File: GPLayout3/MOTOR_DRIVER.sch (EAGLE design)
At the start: 90 parts, among them T1 2N2222, T2 2N2222, U7 ATMEGA328P_TQFP, Y1 16MHz

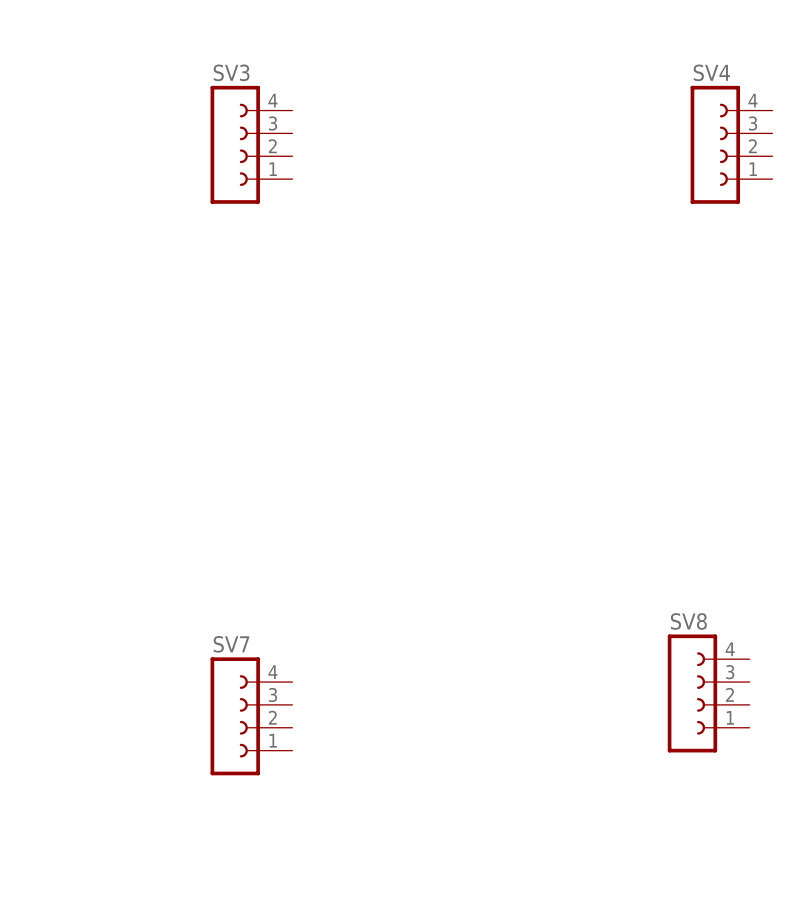
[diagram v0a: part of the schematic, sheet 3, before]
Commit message: Fixed a couple top wires on gate driver chip and gnd
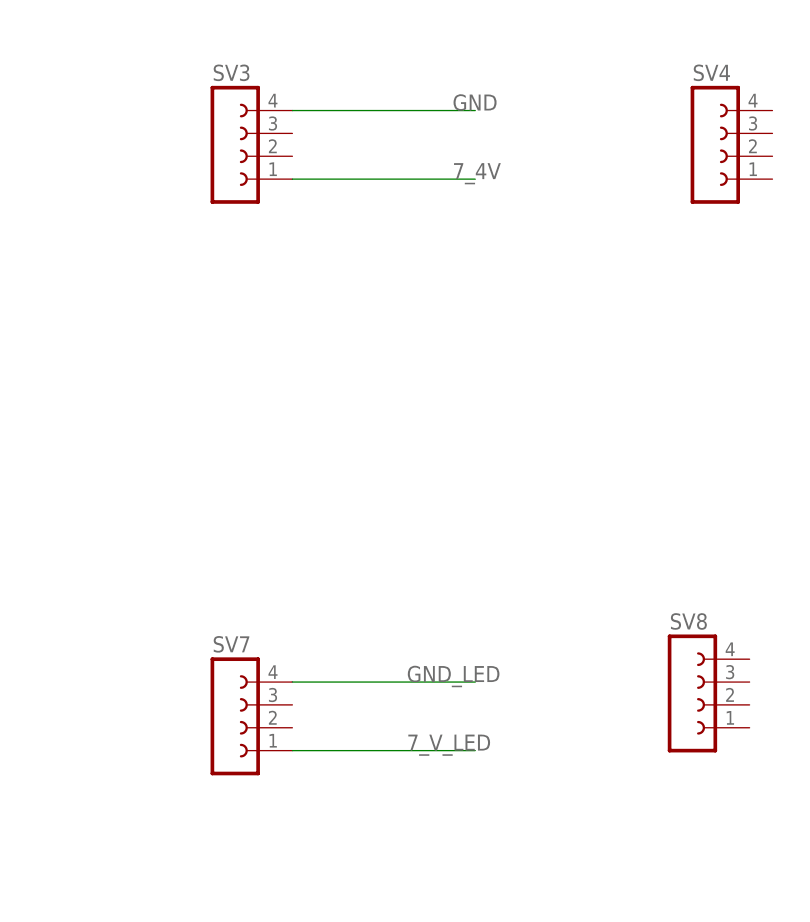
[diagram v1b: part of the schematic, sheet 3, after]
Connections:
- new net 7_V_LED: SV7.1
- new net GND_LED: SV7.4
- net 7_4V: now also SV3.1
- net GND: now also SV3.4
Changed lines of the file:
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@@
 <?xml version="1.0" encoding="utf-8"?>
 <!DOCTYPE eagle SYSTEM "eagle.dtd">
-<eagle version="8.0.1">
+<eagle version="8.0.0">
 <drawing>
 <settings>
@@
 <label x="330.2" y="167.64" size="1.778" layer="95"/>
 </segment>
+<segment>
+<pinref part="SV3" gate="G$1" pin="4"/>
+<wire x1="243.84" y1="226.06" x2="264.16" y2="226.06" width="0.1524" layer="91"/>
+<label x="261.62" y="226.06" size="1.778" layer="95"/>
+</segment>
 </net>
 <net name="5V" class="0">
@@
 <label x="76.2" y="149.86" size="1.778" layer="95"/>
 </segment>
+<segment>
+<pinref part="SV3" gate="G$1" pin="1"/>
+<wire x1="243.84" y1="218.44" x2="264.16" y2="218.44" width="0.1524" layer="91"/>
+<label x="261.62" y="218.44" size="1.778" layer="95"/>
+</segment>
 </net>
 <net name="TX" class="0">
@@
 </segment>
 </net>
+<net name="7_V_LED" class="0">
+<segment>
+<pinref part="SV7" gate="G$1" pin="1"/>
+<wire x1="243.84" y1="154.94" x2="264.16" y2="154.94" width="0.1524" layer="91"/>
+<label x="256.54" y="154.94" size="1.778" layer="95"/>
+</segment>
+</net>
+<net name="GND_LED" class="0">
+<segment>
+<pinref part="SV7" gate="G$1" pin="4"/>
+<wire x1="243.84" y1="162.56" x2="264.16" y2="162.56" width="0.1524" layer="91"/>
+<label x="256.54" y="162.56" size="1.778" layer="95"/>
+</segment>
+</net>

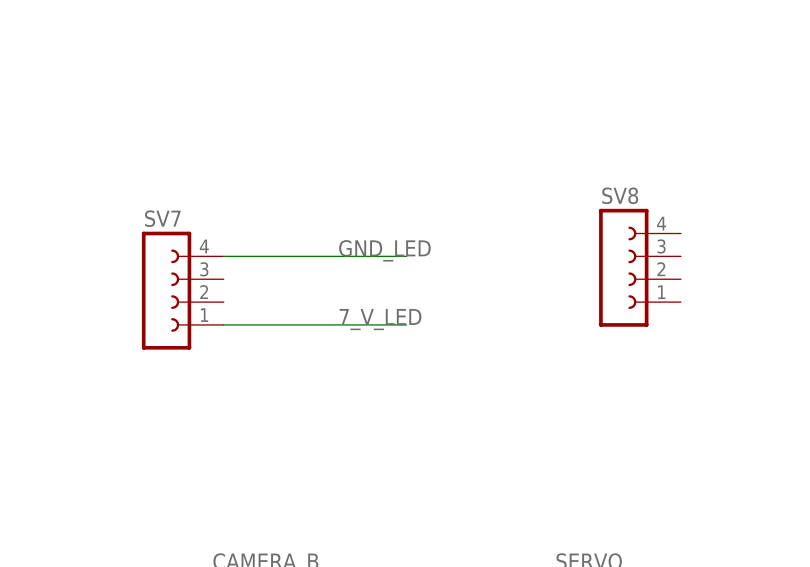
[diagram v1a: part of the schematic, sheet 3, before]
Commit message: Added more wires to top board
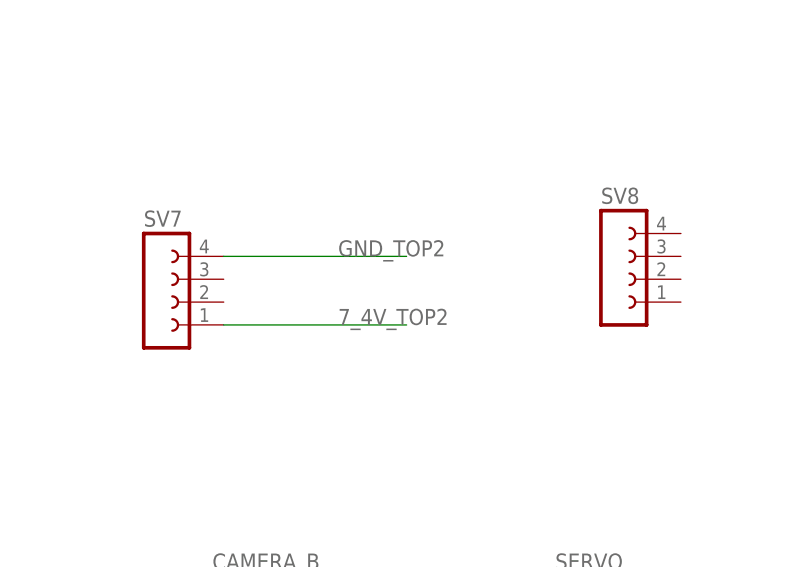
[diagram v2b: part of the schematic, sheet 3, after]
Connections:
- removed net 7_V_LED: SV7.1
- removed net GND_LED: SV7.4
- net 7_4V_TOP2: now also SV7.1
- net GND_TOP2: now also SV7.4
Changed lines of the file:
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@@
 <label x="332.74" y="226.06" size="1.778" layer="95"/>
+</segment>
+<segment>
+<pinref part="SV7" gate="G$1" pin="1"/>
+<wire x1="243.84" y1="154.94" x2="264.16" y2="154.94" width="0.1524" layer="91"/>
+<label x="256.54" y="154.94" size="1.778" layer="95"/>
 </segment>
 </net>
@@
 <wire x1="330.2" y1="223.52" x2="340.36" y2="223.52" width="0.1524" layer="91"/>
 <label x="332.74" y="223.52" size="1.778" layer="95"/>
+</segment>
+<segment>
+<pinref part="SV7" gate="G$1" pin="4"/>
+<wire x1="243.84" y1="162.56" x2="264.16" y2="162.56" width="0.1524" layer="91"/>
+<label x="256.54" y="162.56" size="1.778" layer="95"/>
 </segment>
 </net>
@@
 </segment>
 </net>
-<net name="7_V_LED" class="0">
-<segment>
-<pinref part="SV7" gate="G$1" pin="1"/>
-<wire x1="243.84" y1="154.94" x2="264.16" y2="154.94" width="0.1524" layer="91"/>
-<label x="256.54" y="154.94" size="1.778" layer="95"/>
-</segment>
-</net>
-<net name="GND_LED" class="0">
-<segment>
-<pinref part="SV7" gate="G$1" pin="4"/>
-<wire x1="243.84" y1="162.56" x2="264.16" y2="162.56" width="0.1524" layer="91"/>
-<label x="256.54" y="162.56" size="1.778" layer="95"/>
-</segment>
-</net>

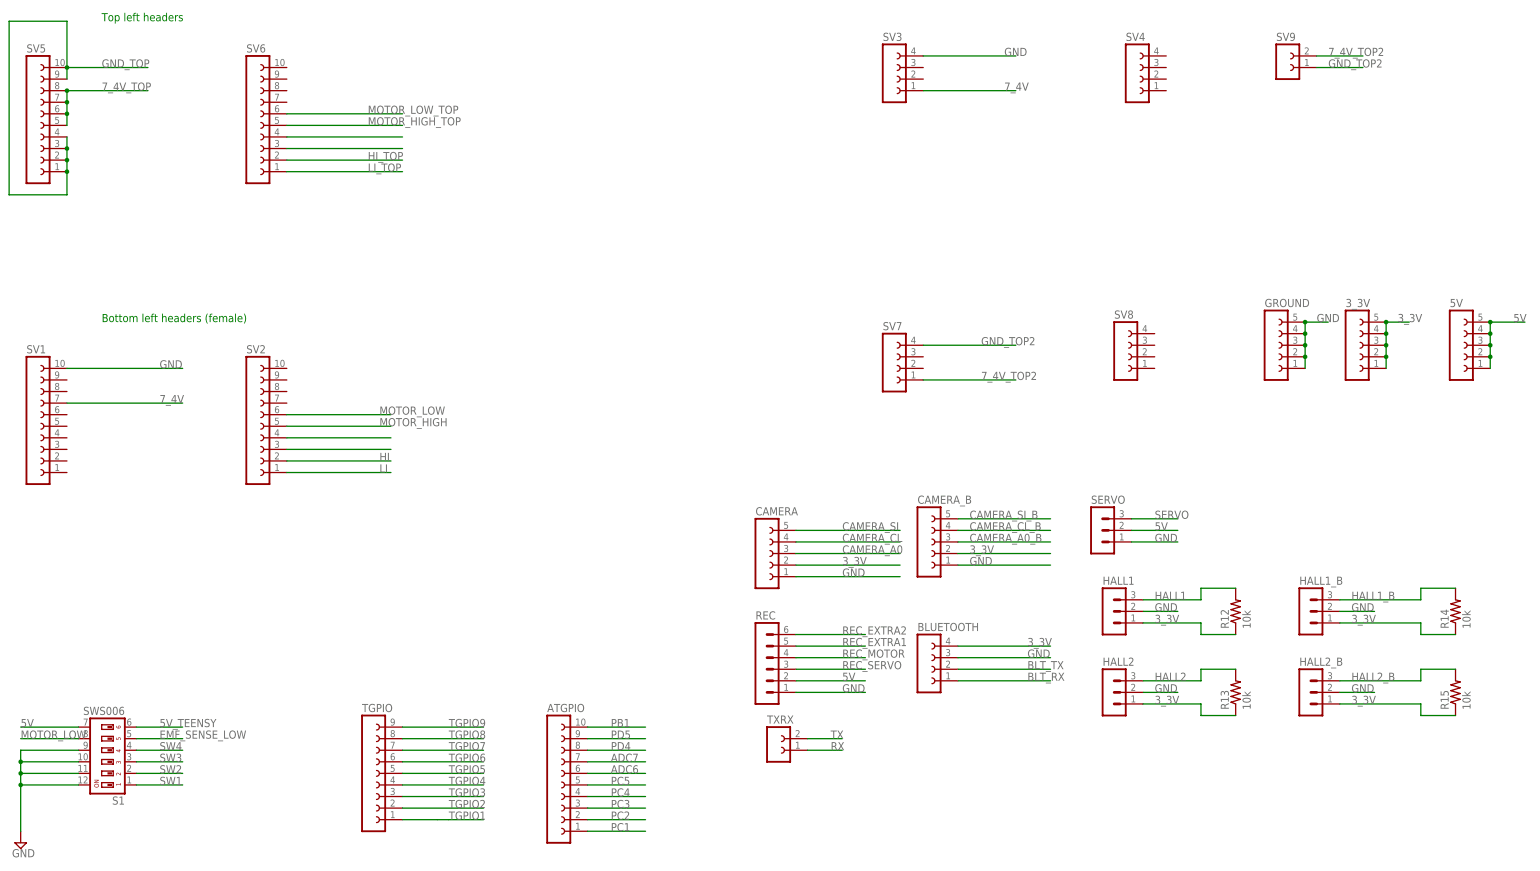
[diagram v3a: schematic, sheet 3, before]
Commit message: Added current sense, needed to change a few pins on upper left. Check routing again. Changed rec header to female
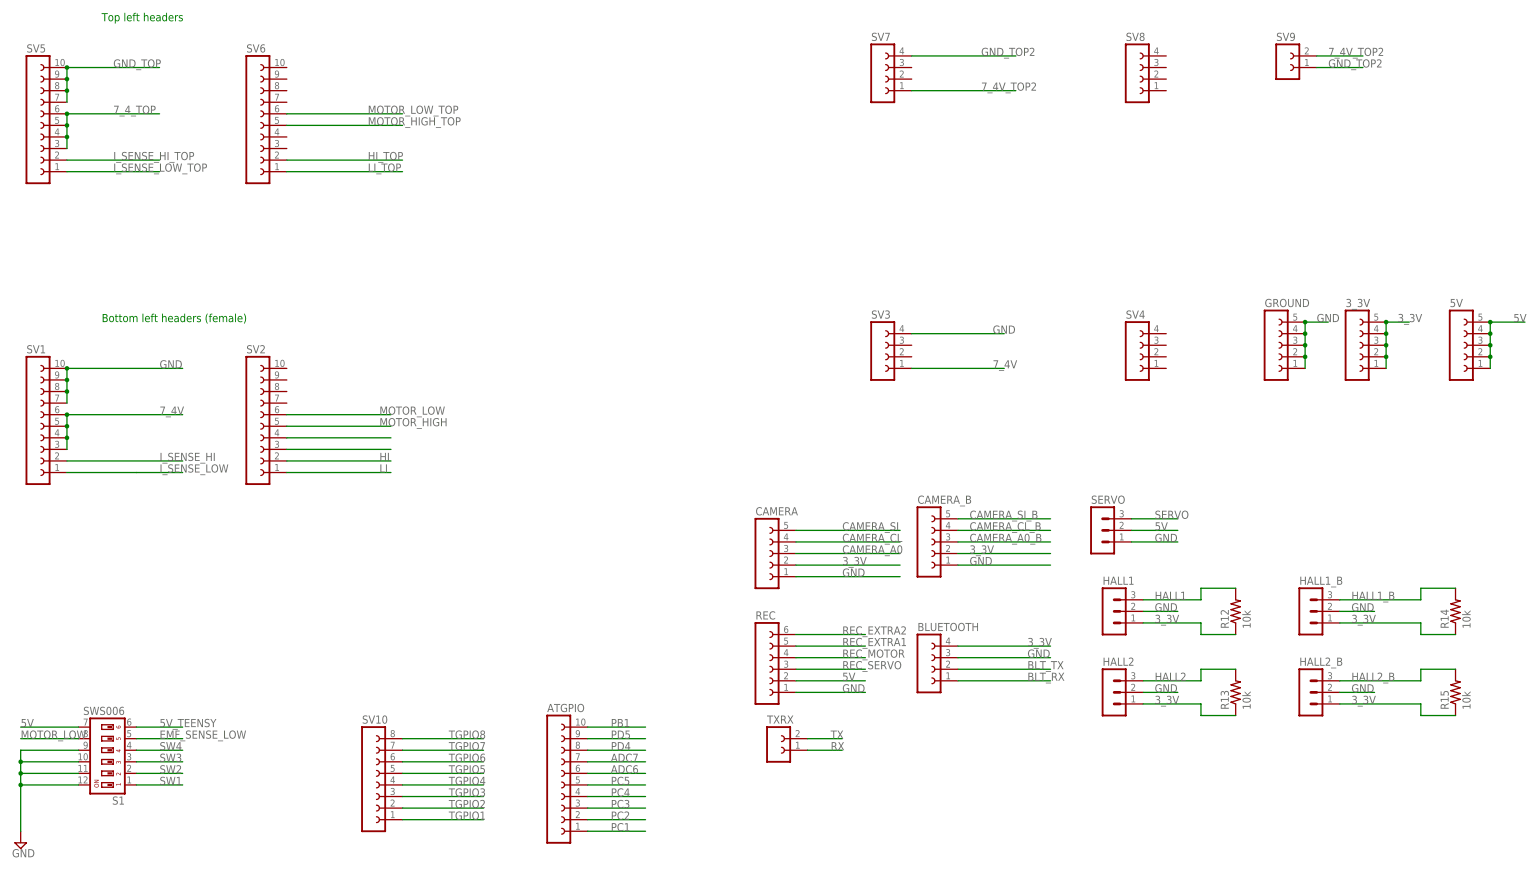
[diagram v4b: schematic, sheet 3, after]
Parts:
- removed TGPIO: (no value), con-lsta:FE09-1
- added C7: (no value), resistor:C-USC0603
- added I_SENSE_AMP: INA138, burr-brown:INA138
- added R17: 10m, rcl:R-US_R2512
- added R18: 10k, rcl:R-US_R0603
- added SV10: (no value), con-lsta:FE08-1
- REC: device con-lstb:MA06-1 -> con-lsta:FE06-1
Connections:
- removed net HI2_TOP: SV6.3
- removed net LI2_TOP: SV6.4
- removed net TGPIO9: TGPIO.9, U$1.A22/DAC1
- new net 7_4_TOP: SV5.3, SV5.4, SV5.5, SV5.6
- new net I_SENSE: I_SENSE_AMP.OUT, R18.2, U$1.A22/DAC1
- new net I_SENSE_HI: I_SENSE_AMP.IN+, SV1.2
- new net I_SENSE_HI_TOP: BOT_REV.DRAIN, R17.1, SV5.2, TOP_FWD.SOURCE
- new net I_SENSE_LOW: I_SENSE_AMP.IN-, SV1.1
- new net I_SENSE_LOW_TOP: MOTOR_POS.MP, R17.2, SV5.1
- net 7_4V: now also C7.1, I_SENSE_AMP.V+, SV1.3, SV1.4, SV1.5, SV1.6; no longer SV1.7
- net 7_4V_TOP: no longer SV5.5, SV5.6, SV5.7, SV5.8
- net GND: now also C7.2, I_SENSE_AMP.V-, R18.1, SV1.7, SV1.8, SV1.9
- net GND_TOP: now also SV5.7, SV5.8; no longer SV5.1, SV5.2, SV5.3, SV5.4
- net MOTOR_HIGH_TOP: no longer BOT_REV.DRAIN, MOTOR_POS.MP, TOP_FWD.SOURCE
- net TGPIO1: now also SV10.1; no longer TGPIO.1
- net TGPIO2: now also SV10.2; no longer TGPIO.2
- net TGPIO3: now also SV10.3; no longer TGPIO.3
- net TGPIO4: now also SV10.4; no longer TGPIO.4
- net TGPIO5: now also SV10.5; no longer TGPIO.5
- net TGPIO6: now also SV10.6; no longer TGPIO.6
- net TGPIO7: now also SV10.7; no longer TGPIO.7
- net TGPIO8: now also SV10.8; no longer TGPIO.8
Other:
- moved on the sheet: MOTOR_POS, SV3, SV4, SV7, SV8

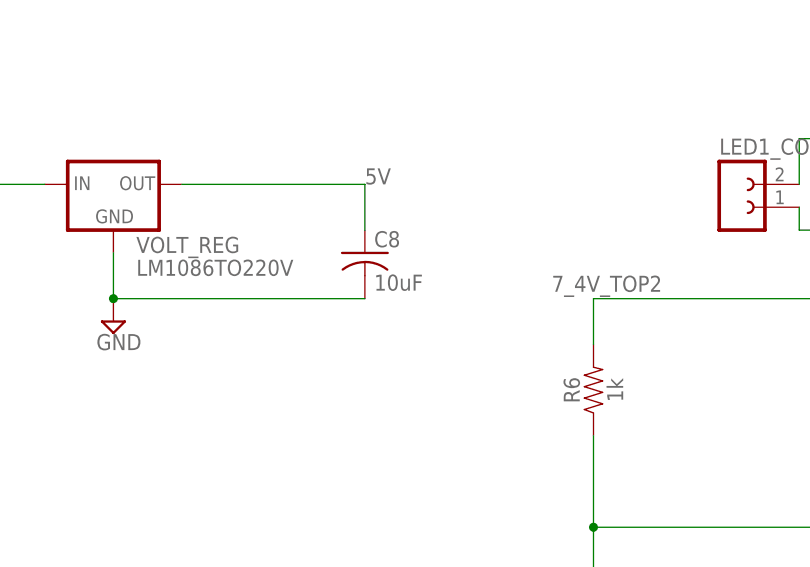
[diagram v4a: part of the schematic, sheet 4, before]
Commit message: changed voltage regulator cap
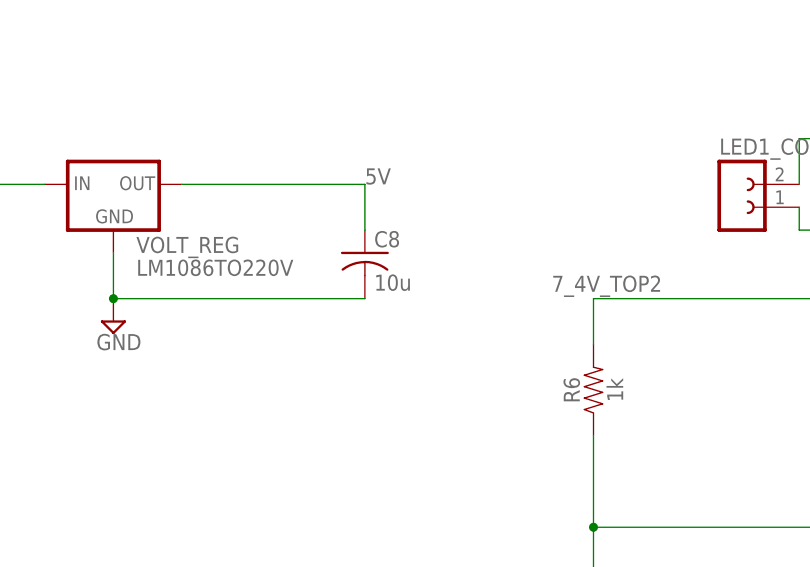
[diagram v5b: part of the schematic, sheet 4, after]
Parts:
- C8: value 10uF -> 10u; device resistor:C-US050-025X075 -> rcl:C-USC0805
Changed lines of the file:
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@@
 <part name="BATT_LOW" library="solpad" deviceset="SE14" device=""/>
 <part name="SUPPLY1" library="supply2" deviceset="GND" device=""/>
-<part name="C8" library="resistor" deviceset="C-US" device="050-025X075" value="10uF"/>
 <part name="C12" library="resistor" deviceset="CPOL-US" device="153CLV-1010" value="33u"/>
 <part name="C13" library="resistor" deviceset="CPOL-US" device="153CLV-1010" value="33u"/>
@@
 <part name="C7" library="resistor" deviceset="C-US" device="C0603"/>
 <part name="REC" library="con-lsta" deviceset="FE06-1" device=""/>
+<part name="C8" library="rcl" deviceset="C-US" device="C0805" value="10u"/>
 </parts>
 <sheets>
@@
 <instance part="BATT_LOW" gate="1" x="78.74" y="165.1" rot="R180"/>
 <instance part="SUPPLY1" gate="GND" x="170.18" y="203.2"/>
-<instance part="C8" gate="G$1" x="198.12" y="210.82"/>
 <instance part="C12" gate="G$1" x="45.72" y="198.12"/>
 <instance part="C13" gate="G$1" x="60.96" y="198.12"/>
@@
 <instance part="LED2_CONN2" gate="G$1" x="297.18" y="218.44"/>
 <instance part="R16" gate="G$1" x="88.9" y="195.58" rot="R90"/>
+<instance part="C8" gate="G$1" x="198.12" y="210.82"/>
 </instances>
 <busses>
@@
 <segment>
 <pinref part="VOLT_REG" gate="G$1" pin="OUT"/>
-<pinref part="C8" gate="G$1" pin="1"/>
 <wire x1="177.8" y1="218.44" x2="198.12" y2="218.44" width="0.1524" layer="91"/>
 <wire x1="198.12" y1="218.44" x2="198.12" y2="213.36" width="0.1524" layer="91"/>
 <label x="198.12" y="218.44" size="1.778" layer="95"/>
+<pinref part="C8" gate="G$1" pin="1"/>
 </segment>
 </net>
 <net name="GND" class="0">
 <segment>
-<pinref part="C8" gate="G$1" pin="2"/>
 <pinref part="SUPPLY1" gate="GND" pin="GND"/>
 <wire x1="198.12" y1="205.74" x2="170.18" y2="205.74" width="0.1524" layer="91"/>
@@
 <wire x1="170.18" y1="210.82" x2="170.18" y2="205.74" width="0.1524" layer="91"/>
 <junction x="170.18" y="205.74"/>
-</segment>
-</net>
+<pinref part="C8" gate="G$1" pin="2"/>
+</segment>
+</net>

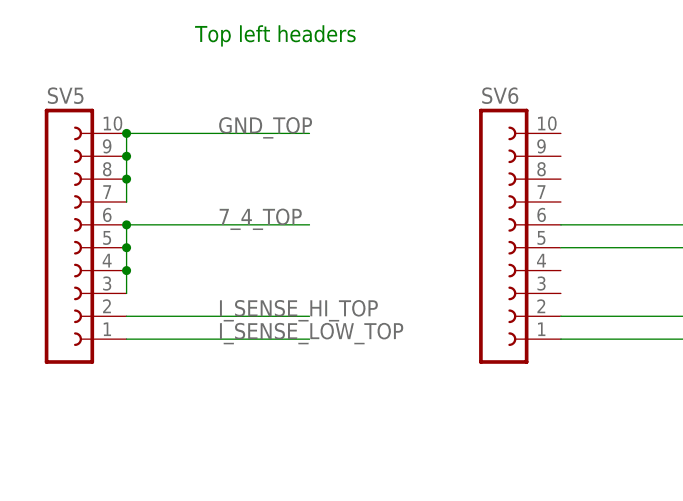
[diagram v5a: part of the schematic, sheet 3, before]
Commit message: Updated top routing to include current sense resistor at 135 degree angle.
4pcb should be checked to see if they can make the pads for the angled
component
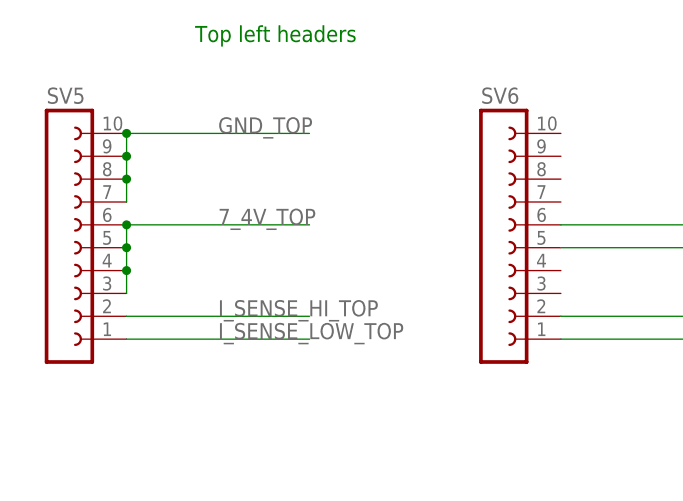
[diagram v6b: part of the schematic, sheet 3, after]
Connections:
- removed net 7_4_TOP: SV5.3, SV5.4, SV5.5, SV5.6
- net 7_4V_TOP: now also SV5.3, SV5.4, SV5.5, SV5.6
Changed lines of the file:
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@@
 <?xml version="1.0" encoding="utf-8"?>
 <!DOCTYPE eagle SYSTEM "eagle.dtd">
-<eagle version="8.0.1">
+<eagle version="8.0.0">
 <drawing>
 <settings>
@@
 </segment>
 </net>
-<net name="7_4_TOP" class="0">
+<net name="7_4V_TOP" class="0">
 <segment>
 <pinref part="SV5" gate="G$1" pin="6"/>
